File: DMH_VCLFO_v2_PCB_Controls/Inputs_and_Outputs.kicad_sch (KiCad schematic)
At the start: 41 parts, among them J13 TS_Jack_6.35mm_Sw, J14 TS_Jack_6.35mm_Sw, J15 TS_Jack_6.35mm_Sw, J16 TS_Jack_6.35mm_Sw, J17 TS_Jack_6.35mm_Sw, J18 TS_Jack_6.35mm_Sw, J29 Conn_01x08, J30 Conn_01x08, J31 IDC_02x05, J32 Conn_01x08, J33 Conn_01x08, Q5 BC548, Q6 BC558, SW10 SPDT_OnOffOn, SW11 SW_SPDT, SW12 SW_SPDT, SW9 SW_SPDT, U3 TL074

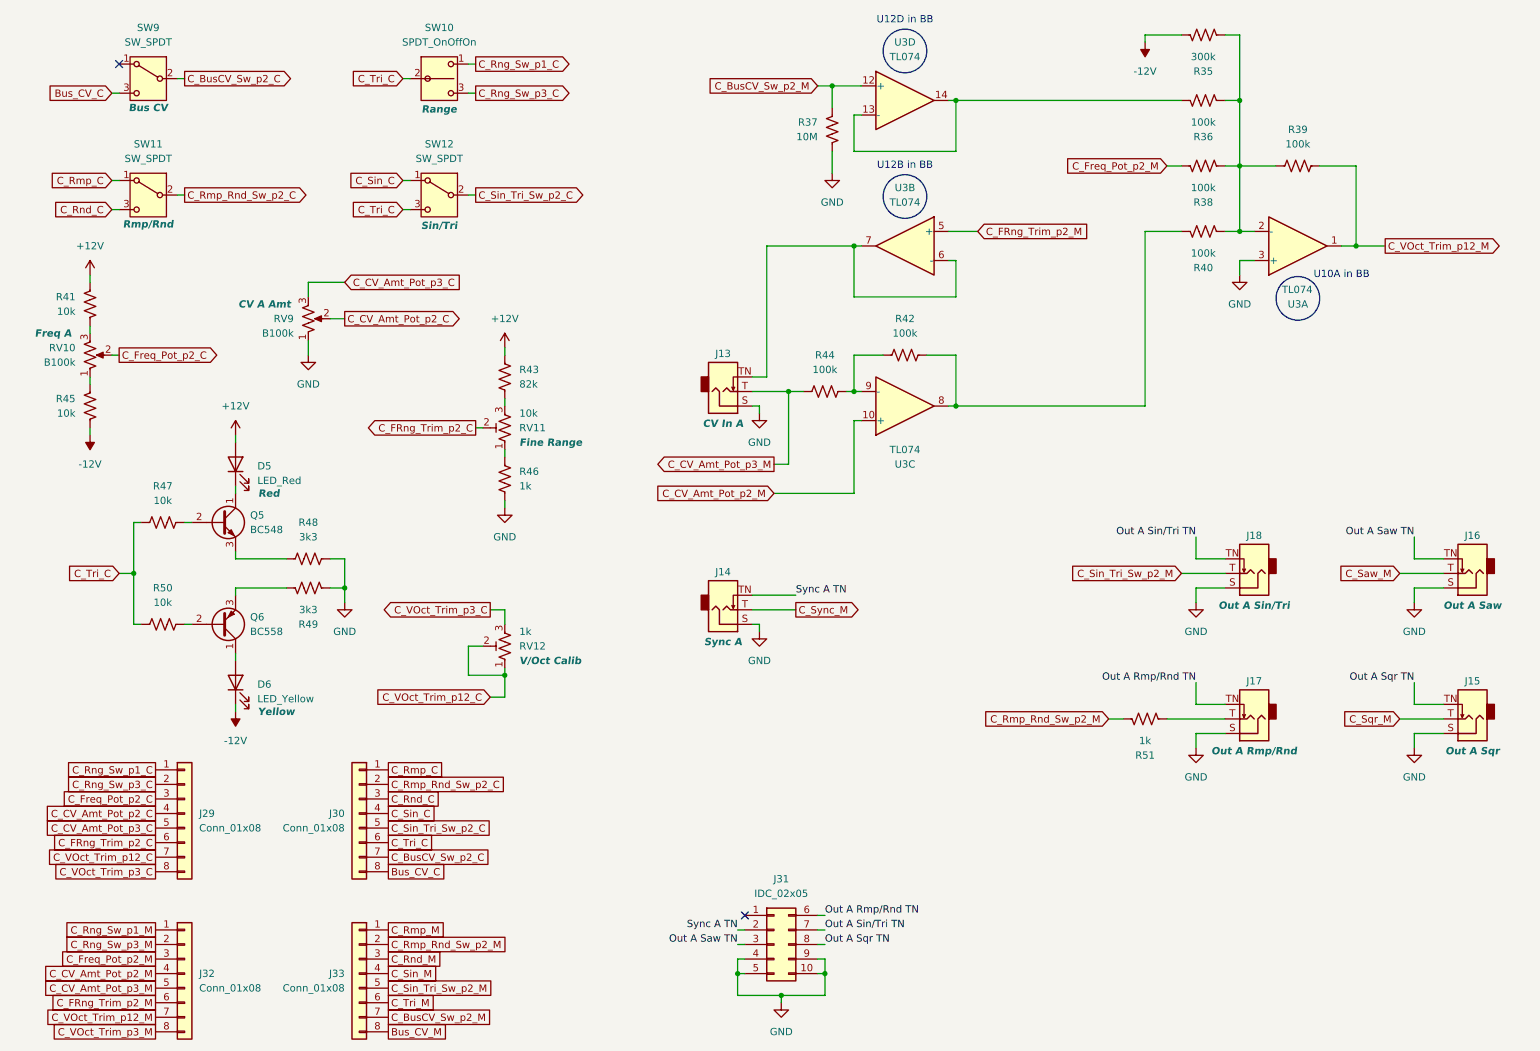
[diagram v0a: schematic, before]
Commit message: Controls PCB comp placement in progress
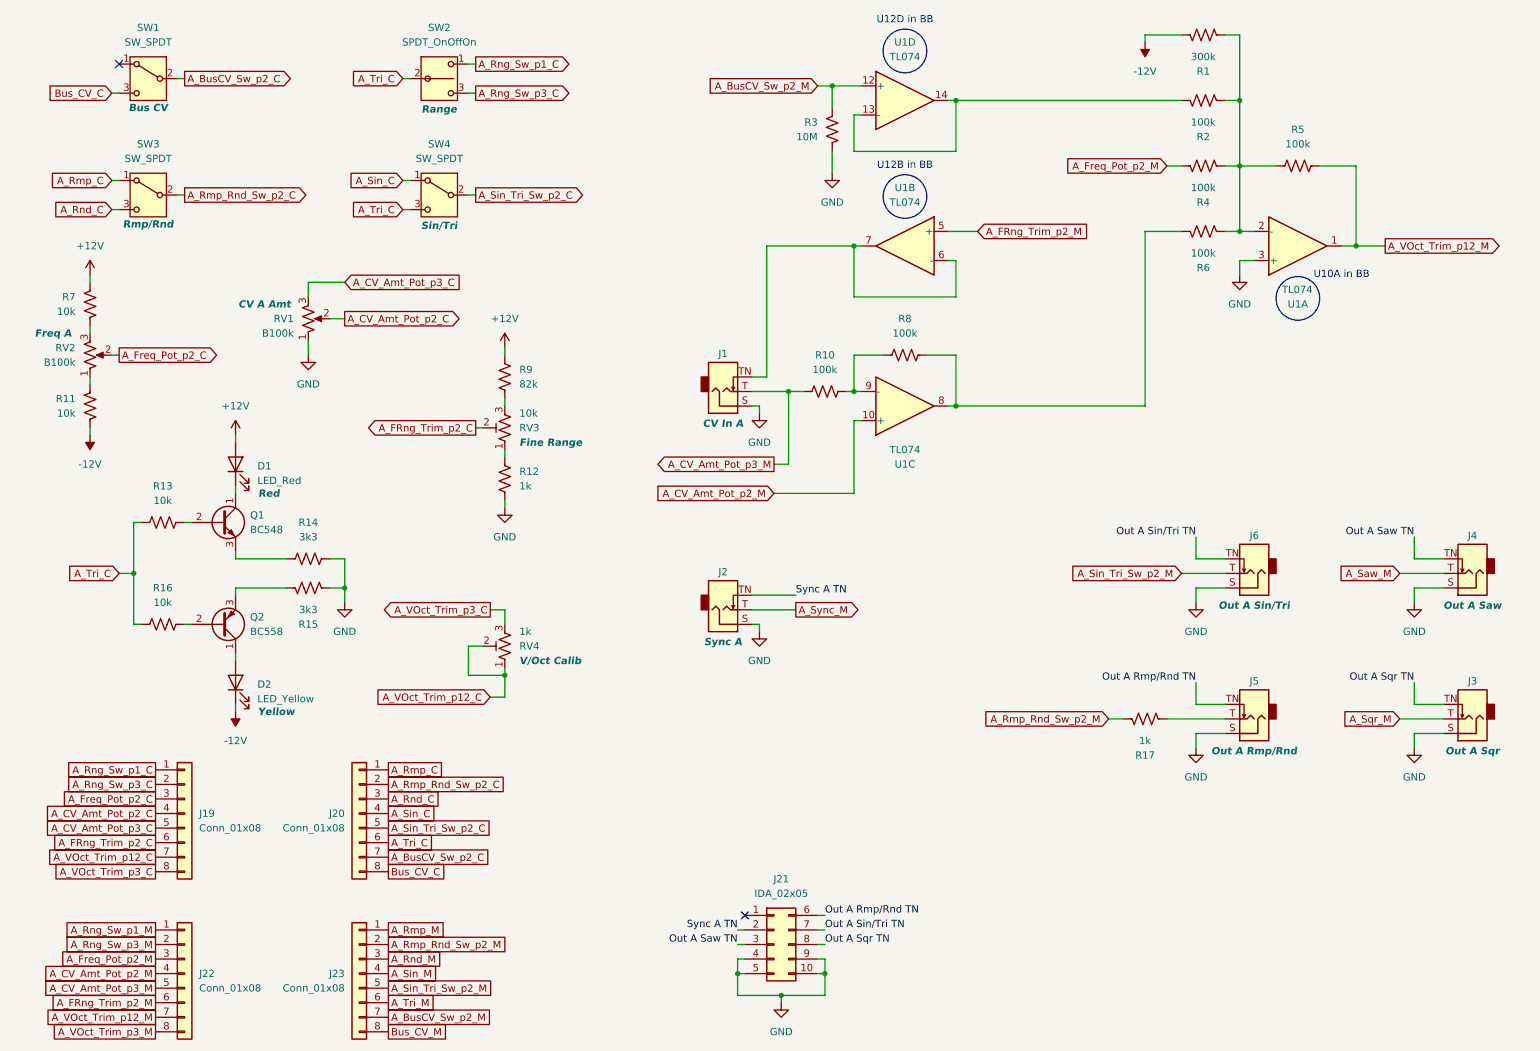
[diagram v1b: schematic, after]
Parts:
- J21: renamed from J31; value IDC_02x05 -> IDA_02x05
- RV1: renamed from RV9; footprint SynthStuff:Potentiometer_Alpha_RD901F-40-00D_Single_Vertical -> SynthStuff:Potentiometer_TT_P110KH1
- RV2: renamed from RV10; footprint SynthStuff:Potentiometer_Alpha_RD901F-40-00D_Single_Vertical -> SynthStuff:Potentiometer_TT_P110KH1
- U1: renamed from U3; footprint Package_DIP:DIP-14_W7.62mm_Socket -> (none)
- renumbered D5 to D1, D6 to D2, J13 to J1, J29 to J19, J14 to J2, J30 to J20, J32 to J22, J33 to J23, J15 to J3, J16 to J4, J17 to J5, J18 to J6, Q5 to Q1, Q6 to Q2, R35 to R1, R44 to R10, R45 to R11, R46 to R12, R47 to R13, R48 to R14, R49 to R15, R50 to R16, R51 to R17, R36 to R2, R37 to R3, R38 to R4, R39 to R5, R40 to R6, R41 to R7, R42 to R8, R43 to R9, RV11 to RV3, RV12 to RV4, SW9 to SW1, SW10 to SW2, SW11 to SW3, SW12 to SW4, U3 to U1
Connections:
- net C_BusCV_Sw_p2_C renamed A_BusCV_Sw_p2_C
- net C_BusCV_Sw_p2_M renamed A_BusCV_Sw_p2_M
- net C_CV_Amt_Pot_p2_C renamed A_CV_Amt_Pot_p2_C
- net C_CV_Amt_Pot_p2_M renamed A_CV_Amt_Pot_p2_M
- net C_CV_Amt_Pot_p3_C renamed A_CV_Amt_Pot_p3_C
- net C_CV_Amt_Pot_p3_M renamed A_CV_Amt_Pot_p3_M
- net C_FRng_Trim_p2_C renamed A_FRng_Trim_p2_C
- net C_FRng_Trim_p2_M renamed A_FRng_Trim_p2_M
- net C_Freq_Pot_p2_C renamed A_Freq_Pot_p2_C
- net C_Freq_Pot_p2_M renamed A_Freq_Pot_p2_M
- net C_Rmp_C renamed A_Rmp_C
- net C_Rmp_M renamed A_Rmp_M
- net C_Rmp_Rnd_Sw_p2_C renamed A_Rmp_Rnd_Sw_p2_C
- net C_Rmp_Rnd_Sw_p2_M renamed A_Rmp_Rnd_Sw_p2_M
- net C_Rnd_C renamed A_Rnd_C
- net C_Rnd_M renamed A_Rnd_M
- net C_Rng_Sw_p1_C renamed A_Rng_Sw_p1_C
- net C_Rng_Sw_p1_M renamed A_Rng_Sw_p1_M
- net C_Rng_Sw_p3_C renamed A_Rng_Sw_p3_C
- net C_Rng_Sw_p3_M renamed A_Rng_Sw_p3_M
- net C_Saw_M renamed A_Saw_M
- net C_Sin_C renamed A_Sin_C
- net C_Sin_M renamed A_Sin_M
- net C_Sin_Tri_Sw_p2_C renamed A_Sin_Tri_Sw_p2_C
- net C_Sin_Tri_Sw_p2_M renamed A_Sin_Tri_Sw_p2_M
- net C_Sqr_M renamed A_Sqr_M
- net C_Sync_M renamed A_Sync_M
- net C_Tri_C renamed A_Tri_C
- net C_Tri_M renamed A_Tri_M
- net C_VOct_Trim_p12_C renamed A_VOct_Trim_p12_C
- net C_VOct_Trim_p12_M renamed A_VOct_Trim_p12_M
- net C_VOct_Trim_p3_C renamed A_VOct_Trim_p3_C
- net C_VOct_Trim_p3_M renamed A_VOct_Trim_p3_M
